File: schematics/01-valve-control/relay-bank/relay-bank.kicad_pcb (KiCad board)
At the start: 4 copper layers, 68.8 x 86.5 mm, 41 parts, among them J102 PWR, J103 EN, J201 VALVE, J301 VALVE, J401 VALVE, J501 VALVE, J601 VALVE, K201 SPST Relay, K301 SPST Relay, K401 SPST Relay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

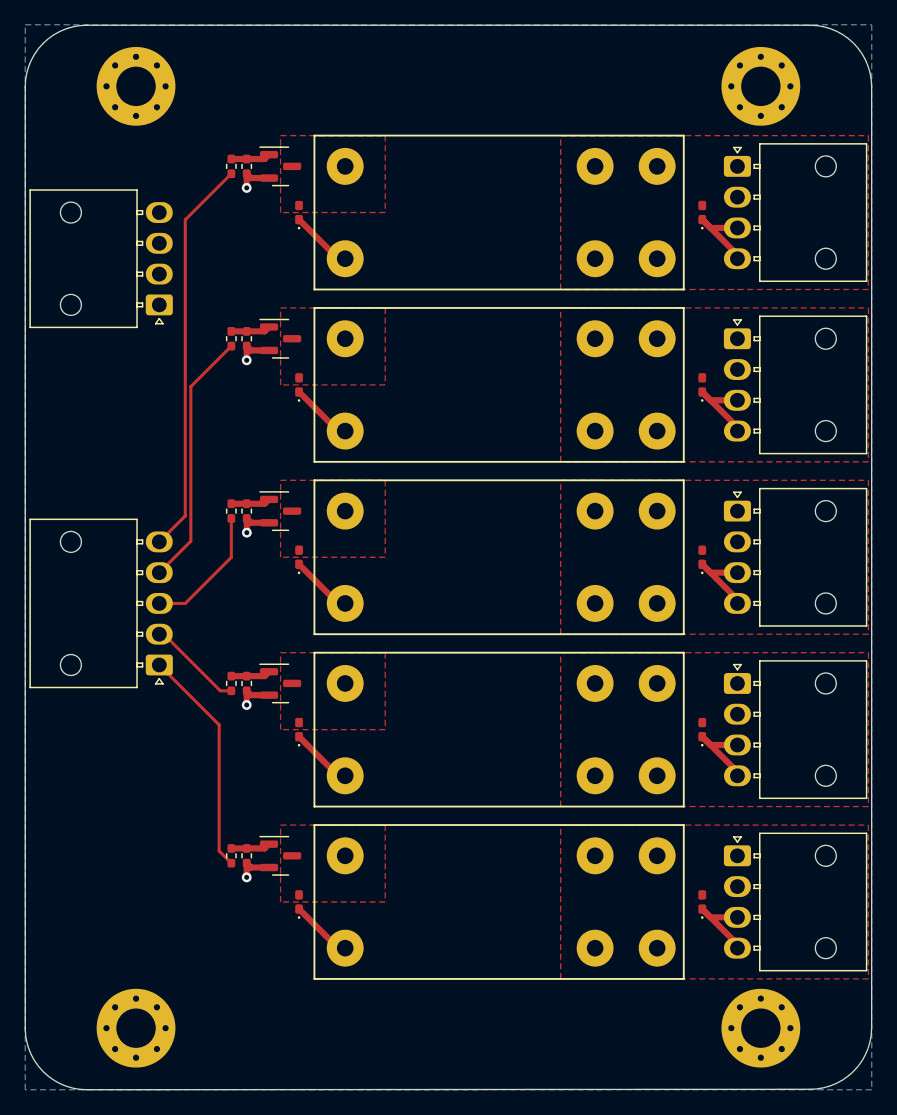
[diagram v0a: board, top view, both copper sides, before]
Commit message: Relay bank changes for manufacture
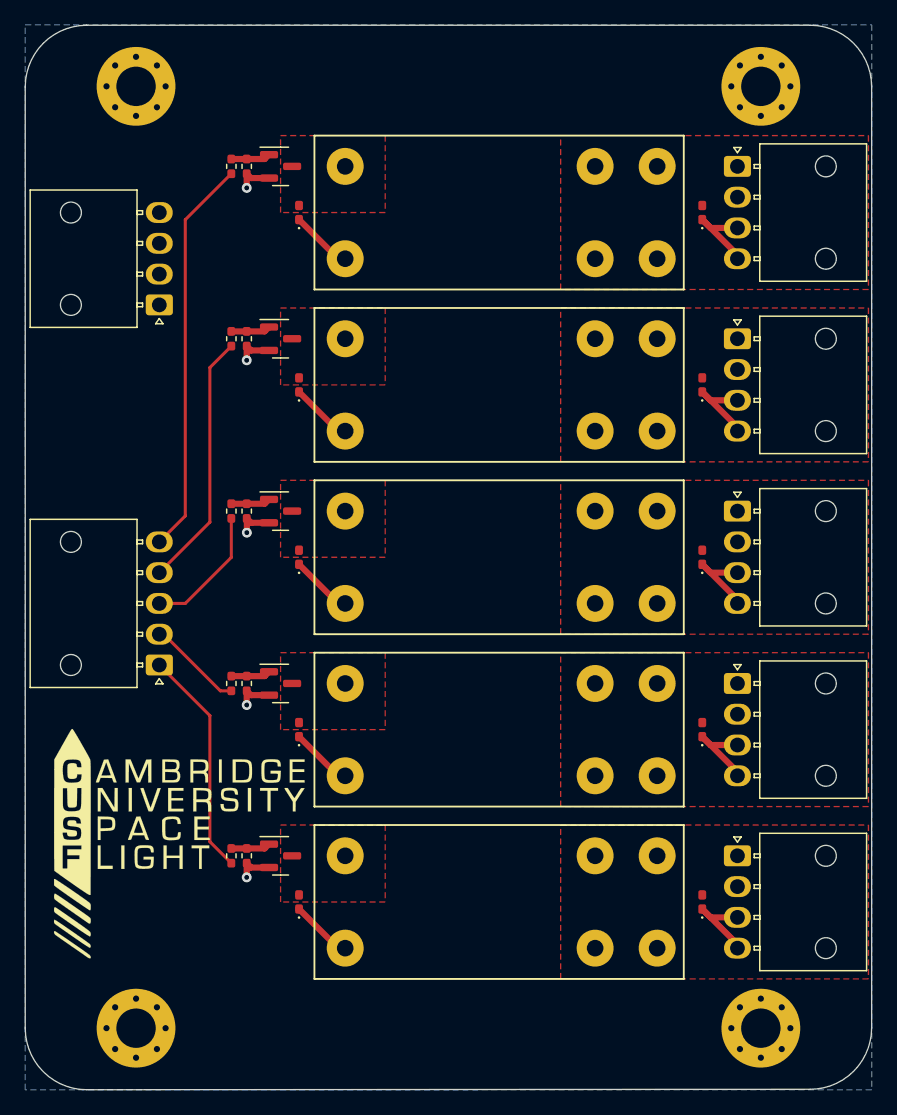
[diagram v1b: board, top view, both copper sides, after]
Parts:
- added G***: LOGO, royale:cusf_logo_full, F.Cu at (135.5, 133.0)
- added G***: LOGO, royale:This_Is_Fine, B.Cu at (158.6, 109.2)
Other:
- board text added: "BANK VOLTAGE"
- board text added: "Designed by H. Franks Jan. 2022"
- board text added: "PROJECT ROYALE RELAY BANK"
